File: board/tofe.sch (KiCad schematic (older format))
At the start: 16 parts, among them P301 TOFE I2C, P302 TOFE-8X, P303 DEBUG, U301 24AA01/24LC01B

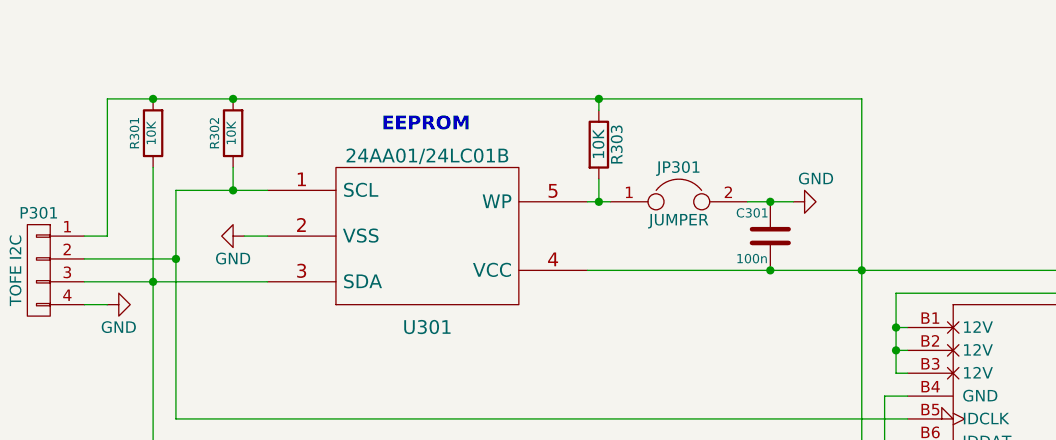
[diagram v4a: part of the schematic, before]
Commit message: Start assigning footprints
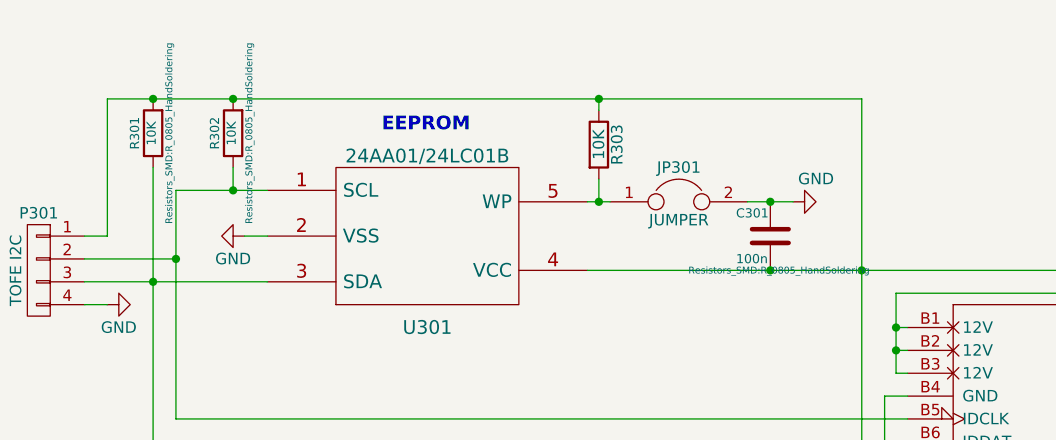
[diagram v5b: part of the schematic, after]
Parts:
- C301, R301, R302: footprint ~ -> Resistors_SMD:R_0805_HandSoldering
- D301, P302, U301: footprint ~ -> (none)
- D302, D303, D304, R303, R304, R305, R306: footprint (none) -> Resistors_SMD:R_0805_HandSoldering
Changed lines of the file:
@@
 F 0 "P302" H 5900 1500 60  0000 C CNN
 F 1 "TOFE-8X" H 5250 1500 60  0000 C CNN
-F 2 "~" H 4600 4050 60  0000 C CNN
+F 2 "" H 4600 4050 60  0001 C CNN
 F 3 "~" H 4600 4050 60  0000 C CNN
 	1    5900 4350
@@
 F 0 "D301" H 6300 1400 40  0000 C CNN
 F 1 "DIODE" H 6300 1200 40  0000 C CNN
-F 2 "~" H 6300 1300 60  0000 C CNN
+F 2 "" H 6300 1300 60  0001 C CNN
 F 3 "~" H 6300 1300 60  0000 C CNN
 	1    6300 1300
@@
 F 0 "U301" H 2500 850 60  0000 C CNN
 F 1 "24AA01/24LC01B" H 2500 1600 60  0000 C CNN
-F 2 "~" H 2500 1250 60  0000 C CNN
+F 2 "" H 2500 1250 60  0001 C CNN
 F 3 "~" H 2500 1250 60  0000 C CNN
 	1    2500 1250
@@
 F 0 "R302" V 1730 800 40  0000 C CNN
 F 1 "10K" V 1657 801 40  0000 C CNN
-F 2 "~" V 1580 800 30  0000 C CNN
+F 2 "Resistors_SMD:R_0805_HandSoldering" V 1580 800 30  0000 C CNN
 F 3 "~" H 1650 800 30  0000 C CNN
 	1    1650 800
@@
 F 0 "R301" V 1380 800 40  0000 C CNN
 F 1 "10K" V 1307 801 40  0000 C CNN
-F 2 "~" V 1230 800 30  0000 C CNN
+F 2 "Resistors_SMD:R_0805_HandSoldering" V 1230 800 30  0000 C CNN
 F 3 "~" H 1300 800 30  0000 C CNN
 	1    1300 800
@@
 F 0 "C301" H 3850 1350 40  0000 L CNN
 F 1 "100n" H 3850 1150 40  0000 L CNN
-F 2 "~" H 4038 1100 30  0000 C CNN
+F 2 "Resistors_SMD:R_0805_HandSoldering" H 4038 1100 30  0000 C CNN
 F 3 "~" H 4000 1250 60  0000 C CNN
 	1    4000 1250
@@
 SDA_VGA_RX
 $Comp
-L GND #PWR304
+L GND #PWR015
 U 1 1 5641057B
 P 5450 7500
-F 0 "#PWR304" H 5450 7250 50  0001 C CNN
+F 0 "#PWR015" H 5450 7250 50  0001 C CNN
 F 1 "GND" H 5450 7350 50  0000 C CNN
 F 2 "" H 5450 7500 60  0000 C CNN
@@
 $EndComp
 $Comp
-L GND #PWR303
+L GND #PWR016
 U 1 1 56410719
 P 4100 1100
-F 0 "#PWR303" H 4100 850 50  0001 C CNN
+F 0 "#PWR016" H 4100 850 50  0001 C CNN
 F 1 "GND" V 4200 1000 50  0000 C CNN
 F 2 "" H 4100 1100 60  0000 C CNN
@@
 $EndComp
 $Comp
-L GND #PWR302
+L GND #PWR017
 U 1 1 564109C3
 P 1700 1250
-F 0 "#PWR302" H 1700 1000 50  0001 C CNN
+F 0 "#PWR017" H 1700 1000 50  0001 C CNN
 F 1 "GND" V 1800 1200 50  0000 C CNN
 F 2 "" H 1700 1250 60  0000 C CNN
@@
 $EndComp
 $Comp
-L +3V3 #PWR305
+L +3V3 #PWR018
 U 1 1 56412B64
 P 5550 1250
-F 0 "#PWR305" H 5550 1100 50  0001 C CNN
+F 0 "#PWR018" H 5550 1100 50  0001 C CNN
 F 1 "+3V3" H 5550 1390 50  0000 C CNN
 F 2 "" H 5550 1250 60  0000 C CNN
@@
 $EndComp
 $Comp
-L +12V #PWR306
+L +12V #PWR019
 U 1 1 56412B95
 P 6700 1250
-F 0 "#PWR306" H 6700 1100 50  0001 C CNN
+F 0 "#PWR019" H 6700 1100 50  0001 C CNN
 F 1 "+12V" H 6700 1390 50  0000 C CNN
 F 2 "" H 6700 1250 60  0000 C CNN
@@
 F 0 "JP301" H 3600 1250 50  0000 C CNN
 F 1 "JUMPER" H 3600 1020 50  0000 C CNN
-F 2 "" H 3600 1100 50  0000 C CNN
+F 2 "" H 3600 1100 50  0001 C CNN
 F 3 "" H 3600 1100 50  0000 C CNN
 	1    3600 1100
@@
 	6550 3250 6800 3250
 $Comp
-L VDD #PWR307
+L VDD #PWR020
 U 1 1 56925C2E
 P 8550 2950
-F 0 "#PWR307" H 8550 2800 50  0001 C CNN
+F 0 "#PWR020" H 8550 2800 50  0001 C CNN
 F 1 "VDD" H 8550 3100 50  0000 C CNN
 F 2 "" H 8550 2950 50  0000 C CNN
@@
 F 0 "D302" H 8350 3100 50  0000 C CNN
 F 1 "LED" H 8100 2950 50  0001 C CNN
-F 2 "" H 8100 3050 50  0000 C CNN
+F 2 "Resistors_SMD:R_0805_HandSoldering" H 8100 3050 50  0001 C CNN
 F 3 "" H 8100 3050 50  0000 C CNN
 	1    8100 3050
@@
 F 0 "R304" V 7500 3300 50  0000 C CNN
 F 1 "68R" V 7550 3050 50  0000 C CNN
-F 2 "" V 7480 3050 50  0000 C CNN
+F 2 "Resistors_SMD:R_0805_HandSoldering" V 7480 3050 50  0001 C CNN
 F 3 "" H 7550 3050 50  0000 C CNN
 	1    7550 3050
@@
 F 0 "D303" H 8350 3200 50  0000 C CNN
 F 1 "LED" H 8100 3050 50  0001 C CNN
-F 2 "" H 8100 3150 50  0000 C CNN
+F 2 "Resistors_SMD:R_0805_HandSoldering" H 8100 3150 50  0001 C CNN
 F 3 "" H 8100 3150 50  0000 C CNN
 	1    8100 3150
@@
 F 0 "R305" V 7500 3400 50  0000 C CNN
 F 1 "68R" V 7550 3150 50  0000 C CNN
-F 2 "" V 7480 3150 50  0000 C CNN
+F 2 "Resistors_SMD:R_0805_HandSoldering" V 7480 3150 50  0001 C CNN
 F 3 "" H 7550 3150 50  0000 C CNN
 	1    7550 3150
@@
 F 0 "D304" H 8350 3300 50  0000 C CNN
 F 1 "LED" H 8100 3150 50  0001 C CNN
-F 2 "" H 8100 3250 50  0000 C CNN
+F 2 "Resistors_SMD:R_0805_HandSoldering" H 8100 3250 50  0001 C CNN
 F 3 "" H 8100 3250 50  0000 C CNN
 	1    8100 3250
@@
 F 0 "R306" V 7500 3500 50  0000 C CNN
 F 1 "68R" V 7550 3250 50  0000 C CNN
-F 2 "" V 7480 3250 50  0000 C CNN
+F 2 "Resistors_SMD:R_0805_HandSoldering" V 7480 3250 50  0001 C CNN
 F 3 "" H 7550 3250 50  0000 C CNN
 	1    7550 3250
@@
 F 0 "P301" H 800 1650 50  0000 C CNN
 F 1 "TOFE I2C" V 900 1400 50  0000 C CNN
-F 2 "" H 800 1400 50  0000 C CNN
+F 2 "" H 800 1400 50  0001 C CNN
 F 3 "" H 800 1400 50  0000 C CNN
 	1    800  1400
@@
 Connection ~ 1400 1350
 $Comp
-L GND #PWR301
+L GND #PWR021
 U 1 1 56931407
 P 1100 1550
-F 0 "#PWR301" H 1100 1300 50  0001 C CNN
+F 0 "#PWR021" H 1100 1300 50  0001 C CNN
 F 1 "GND" V 1000 1500 50  0000 C CNN
 F 2 "" H 1100 1550 50  0000 C CNN
@@
 F 0 "R303" V 3330 850 50  0000 C CNN
 F 1 "10K" V 3250 850 50  0000 C CNN
-F 2 "" V 3180 850 50  0000 C CNN
+F 2 "Resistors_SMD:R_0805_HandSoldering" V 3180 850 50  0001 C CNN
 F 3 "" H 3250 850 50  0000 C CNN
 	1    3250 850
@@
 F 0 "P303" H 7050 3350 50  0000 C CNN
 F 1 "DEBUG" H 7050 2850 50  0000 C CNN
-F 2 "" H 7050 1900 50  0000 C CNN
+F 2 "" H 7050 1900 50  0001 C CNN
 F 3 "" H 7050 1900 50  0000 C CNN
 	1    7050 3100

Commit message: More footprint assigning and generated Netlist
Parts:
- D302, D303, D304: footprint Resistors_SMD:R_0805_HandSoldering -> LEDs:LED_0805
- P302: footprint (none) -> TOFE_8X_HalfHeight:TOFE_8X_HalfHeight
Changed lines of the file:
@@
 F 0 "P302" H 5900 1500 60  0000 C CNN
 F 1 "TOFE-8X" H 5250 1500 60  0000 C CNN
-F 2 "" H 4600 4050 60  0001 C CNN
+F 2 "TOFE_8X_HalfHeight:TOFE_8X_HalfHeight" H 4600 4050 60  0001 C CNN
 F 3 "~" H 4600 4050 60  0000 C CNN
 	1    5900 4350
@@
 F 0 "D302" H 8350 3100 50  0000 C CNN
 F 1 "LED" H 8100 2950 50  0001 C CNN
-F 2 "Resistors_SMD:R_0805_HandSoldering" H 8100 3050 50  0001 C CNN
+F 2 "LEDs:LED_0805" H 8100 3050 50  0001 C CNN
 F 3 "" H 8100 3050 50  0000 C CNN
 	1    8100 3050
@@
 F 0 "D303" H 8350 3200 50  0000 C CNN
 F 1 "LED" H 8100 3050 50  0001 C CNN
-F 2 "Resistors_SMD:R_0805_HandSoldering" H 8100 3150 50  0001 C CNN
+F 2 "LEDs:LED_0805" H 8100 3150 50  0001 C CNN
 F 3 "" H 8100 3150 50  0000 C CNN
 	1    8100 3150
@@
 F 0 "D304" H 8350 3300 50  0000 C CNN
 F 1 "LED" H 8100 3150 50  0001 C CNN
-F 2 "Resistors_SMD:R_0805_HandSoldering" H 8100 3250 50  0001 C CNN
+F 2 "LEDs:LED_0805" H 8100 3250 50  0001 C CNN
 F 3 "" H 8100 3250 50  0000 C CNN
 	1    8100 3250

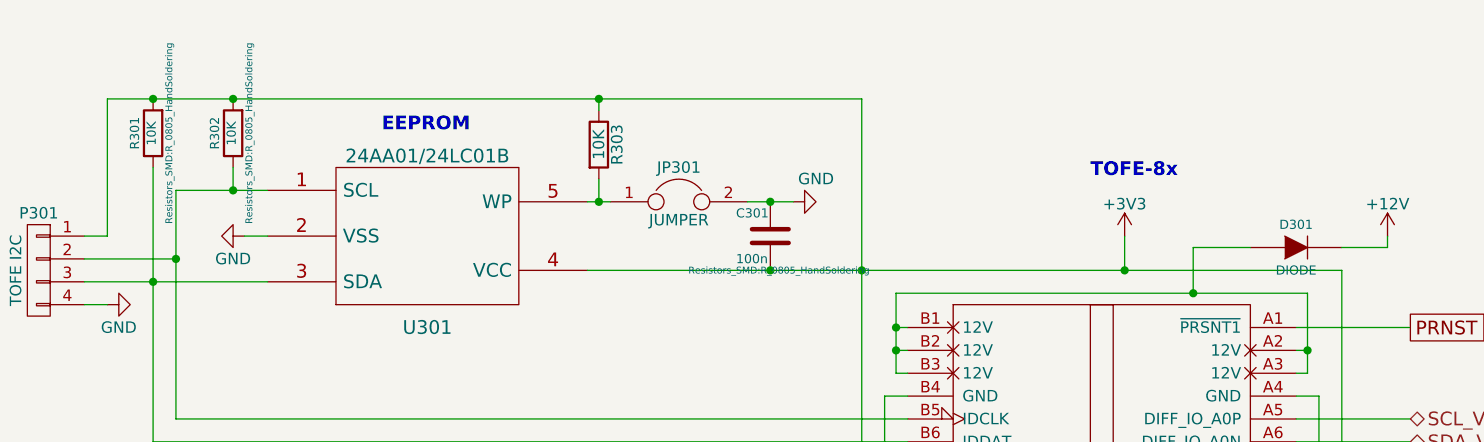
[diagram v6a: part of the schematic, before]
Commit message: More footprint assigning
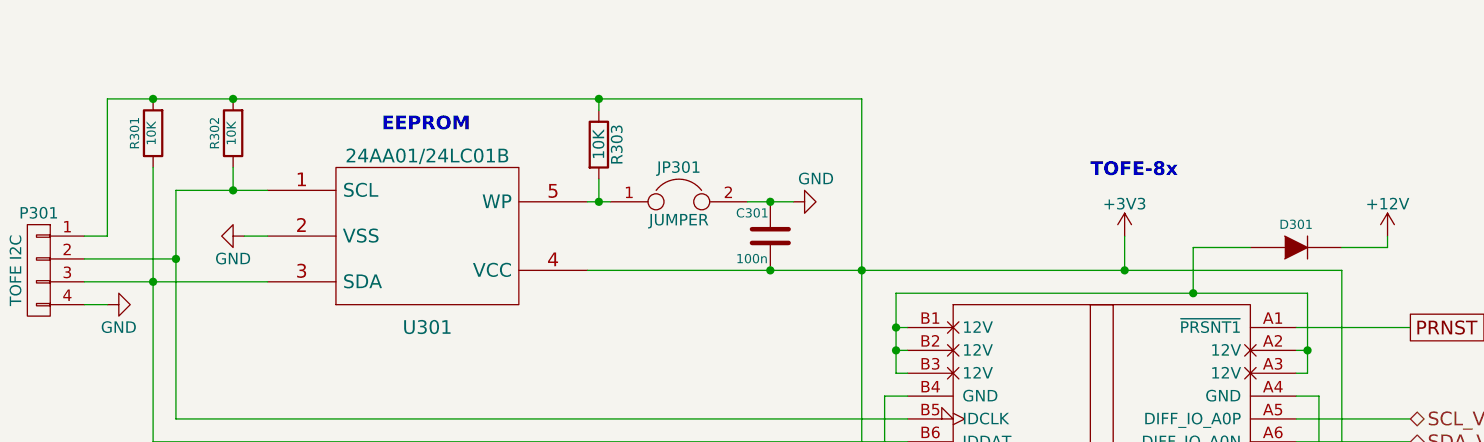
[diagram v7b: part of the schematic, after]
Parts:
- JP301: footprint (none) -> CON-2X1-2.54:CON-2X1-2.54
- P301: footprint (none) -> CON-4X1-2.54:CON-2X1-2.54
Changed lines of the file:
@@
 P 6300 1300
 F 0 "D301" H 6300 1400 40  0000 C CNN
-F 1 "DIODE" H 6300 1200 40  0000 C CNN
+F 1 "DIODE" H 6300 1200 40  0001 C CNN
 F 2 "" H 6300 1300 60  0001 C CNN
 F 3 "~" H 6300 1300 60  0000 C CNN
@@
 F 0 "R302" V 1730 800 40  0000 C CNN
 F 1 "10K" V 1657 801 40  0000 C CNN
-F 2 "Resistors_SMD:R_0805_HandSoldering" V 1580 800 30  0000 C CNN
+F 2 "Resistors_SMD:R_0805_HandSoldering" V 1580 800 30  0001 C CNN
 F 3 "~" H 1650 800 30  0000 C CNN
 	1    1650 800
@@
 F 0 "R301" V 1380 800 40  0000 C CNN
 F 1 "10K" V 1307 801 40  0000 C CNN
-F 2 "Resistors_SMD:R_0805_HandSoldering" V 1230 800 30  0000 C CNN
+F 2 "Resistors_SMD:R_0805_HandSoldering" V 1230 800 30  0001 C CNN
 F 3 "~" H 1300 800 30  0000 C CNN
 	1    1300 800
@@
 F 0 "C301" H 3850 1350 40  0000 L CNN
 F 1 "100n" H 3850 1150 40  0000 L CNN
-F 2 "Resistors_SMD:R_0805_HandSoldering" H 4038 1100 30  0000 C CNN
+F 2 "Resistors_SMD:R_0805_HandSoldering" H 4038 1100 30  0001 C CNN
 F 3 "~" H 4000 1250 60  0000 C CNN
 	1    4000 1250
@@
 F 0 "JP301" H 3600 1250 50  0000 C CNN
 F 1 "JUMPER" H 3600 1020 50  0000 C CNN
-F 2 "" H 3600 1100 50  0001 C CNN
+F 2 "CON-2X1-2.54:CON-2X1-2.54" H 3600 1100 50  0001 C CNN
 F 3 "" H 3600 1100 50  0000 C CNN
 	1    3600 1100
@@
 F 0 "P301" H 800 1650 50  0000 C CNN
 F 1 "TOFE I2C" V 900 1400 50  0000 C CNN
-F 2 "" H 800 1400 50  0001 C CNN
+F 2 "CON-4X1-2.54:CON-2X1-2.54" H 800 1400 50  0001 C CNN
 F 3 "" H 800 1400 50  0000 C CNN
 	1    800  1400

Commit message: More footprints
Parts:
- D301: footprint (none) -> Diodes_SMD:SMB_Handsoldering
- JP301: footprint CON-2X1-2.54:CON-2X1-2.54 -> CON-SMD-2.54:CON-2X1-2.54
- U301: footprint (none) -> TO_SOT_Packages_SMD:SOT-23-5
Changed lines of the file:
@@
 LIBS:testpoint
 LIBS:ad9984-power
+LIBS:3-rca
 EELAYER 25 0
 EELAYER END
@@
 F 0 "D301" H 6300 1400 40  0000 C CNN
 F 1 "DIODE" H 6300 1200 40  0001 C CNN
-F 2 "" H 6300 1300 60  0001 C CNN
+F 2 "Diodes_SMD:SMB_Handsoldering" H 6300 1300 60  0001 C CNN
 F 3 "~" H 6300 1300 60  0000 C CNN
 	1    6300 1300
@@
 F 0 "U301" H 2500 850 60  0000 C CNN
 F 1 "24AA01/24LC01B" H 2500 1600 60  0000 C CNN
-F 2 "" H 2500 1250 60  0001 C CNN
+F 2 "TO_SOT_Packages_SMD:SOT-23-5" H 2500 1250 60  0001 C CNN
 F 3 "~" H 2500 1250 60  0000 C CNN
 	1    2500 1250
@@
 F 0 "JP301" H 3600 1250 50  0000 C CNN
 F 1 "JUMPER" H 3600 1020 50  0000 C CNN
-F 2 "CON-2X1-2.54:CON-2X1-2.54" H 3600 1100 50  0001 C CNN
+F 2 "CON-SMD-2.54:CON-2X1-2.54" H 3600 1100 50  0001 C CNN
 F 3 "" H 3600 1100 50  0000 C CNN
 	1    3600 1100
